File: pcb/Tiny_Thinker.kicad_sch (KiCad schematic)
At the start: 42 parts, among them J2 PERIPHERALS, J3 ADC_TIM, J8 USB_C_Receptacle_USB2.0_16P, SW1 SW_Push, SW2 SW_SPDT, U1 STM32F446RET6, U2 AMS1117-3.3, Y1 16MHz

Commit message: i forgot to save again
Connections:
- net +3.3V: now also J2.10 (Pin_10), J2.18 (Pin_18), J2.38 (Pin_38), J2.9 (Pin_9), J3.37 (Pin_37), J3.40 (Pin_40); no longer J2.13 (Pin_13), J2.14 (Pin_14), J2.25 (Pin_25)
- net CAN1_RX: now also J2.32 (Pin_32); no longer J2.24 (Pin_24)
- net CAN1_TX: now also J2.34 (Pin_34); no longer J2.26 (Pin_26)
- net GND: now also J2.16 (Pin_16), J2.36 (Pin_36), J2.39 (Pin_39), J2.40 (Pin_40), J2.7 (Pin_7), J3.38 (Pin_38), J3.39 (Pin_39); no longer J2.10 (Pin_10), J2.11 (Pin_11), J2.12 (Pin_12), J2.23 (Pin_23), J2.31 (Pin_31), J2.32 (Pin_32)
- net I2C1_SCL: now also J2.23 (Pin_23), J2.24 (Pin_24); no longer J2.15 (Pin_15), J2.16 (Pin_16)
- net I2C1_SDA: now also J2.25 (Pin_25), J2.26 (Pin_26); no longer J2.17 (Pin_17), J2.18 (Pin_18)
- net SPI1_MISO: now also J2.15 (Pin_15); no longer J2.7 (Pin_7)
- net SPI1_MOSI: now also J2.17 (Pin_17); no longer J2.9 (Pin_9)
- net SPI1_NSS: now also J2.11 (Pin_11); no longer J2.3 (Pin_3)
- net SPI1_SCK: now also J2.13 (Pin_13); no longer J2.5 (Pin_5)
- net USB_D+: now also D2.3 (I/O2), J8.A6 (D+), J8.B6 (D+)
- net USB_D-: now also D2.1 (I/O1), J8.A7 (D-), J8.B7 (D-)
- net SPI2_NSS: now reaches U1.33 (PB12)
- net SPI2_NSS: now also J2.37 (Pin_37)
- net SPI2_SCK: now reaches U1.34 (PB13)
- net SPI2_SCK: now also J2.35 (Pin_35)
- net SPI2_MISO: now reaches U1.35 (PB14)
- net SPI2_MISO: now also J2.33 (Pin_33)
- net SPI2_MOSI: now reaches U1.36 (PB15)
- net SPI2_MOSI: now also J2.31 (Pin_31)
- net PA15: now reaches U1.50 (PA15)
- net PA15: now also J2.3 (Pin_3)
- net PC10: now reaches U1.51 (PC10)
- net PC10: now also J2.5 (Pin_5)
- net PC11: now reaches U1.52 (PC11)
- net PC11: now also J2.12 (Pin_12)
- net PC12: now reaches U1.53 (PC12)
- net PC12: now also J2.14 (Pin_14)
- no-connect marks 25 -> 17

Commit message: updated bom / added JLC part #
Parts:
- C16, C17: JLCPCB Part # (none) -> C1623
- D2: JLCPCB Part # (none) -> C7519
- J2, J3: JLCPCB Part # (none) -> C50980
- J8: JLCPCB Part # (none) -> C2765186
- R3: JLCPCB Part # (none) -> C25900
- R4: JLCPCB Part # (none) -> C25531
- R5: JLCPCB Part # (none) -> C17168
- R6, R7: JLCPCB Part # (none) -> C25905
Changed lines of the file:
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@@
 			)
 		)
+		(property "JLCPCB Part #" "C25900"
+			(at 198.12 161.29 0)
+			(effects
+				(font
+					(size 1.27 1.27)
+				)
+				(hide yes)
+			)
+		)
 		(pin "2"
 		)
@@
 			)
 		)
+		(property "JLCPCB Part #" "C2765186"
+			(at 350.52 57.15 0)
+			(effects
+				(font
+					(size 1.27 1.27)
+				)
+				(hide yes)
+			)
+		)
 		(pin "A8"
 		)
@@
 			)
 		)
+		(property "JLCPCB Part #" "C25905"
+			(at 323.85 76.2 0)
+			(effects
+				(font
+					(size 1.27 1.27)
+				)
+				(hide yes)
+			)
+		)
 		(pin "1"
 		)
@@
 			)
 		)
+		(property "JLCPCB Part #" "C25905"
+			(at 332.74 76.2 0)
+			(effects
+				(font
+					(size 1.27 1.27)
+				)
+				(hide yes)
+			)
+		)
 		(pin "1"
 		)
@@
 			)
 		)
+		(property "JLCPCB Part #" "C25531"
+			(at 198.12 171.45 0)
+			(effects
+				(font
+					(size 1.27 1.27)
+				)
+				(hide yes)
+			)
+		)
 		(pin "2"
 		)
@@
 			)
 		)
+		(property "JLCPCB Part #" "C17168"
+			(at 283.21 41.91 90)
+			(effects
+				(font
+					(size 1.27 1.27)
+				)
+				(hide yes)
+			)
+		)
 		(pin "1"
 		)
@@
 			)
 		)
+		(property "JLCPCB Part #" " C7519"
+			(at 320.04 57.15 0)
+			(effects
+				(font
+					(size 1.27 1.27)
+				)
+				(hide yes)
+			)
+		)
 		(pin "3"
 		)
@@
 			)
 		)
+		(property "JLCPCB Part #" " C50980"
+			(at 334.01 181.61 0)
+			(effects
+				(font
+					(size 1.27 1.27)
+				)
+				(hide yes)
+			)
+		)
 		(pin "14"
 		)
@@
 			)
 		)
+		(property "JLCPCB Part #" "C1623"
+			(at 292.1 50.8 0)
+			(effects
+				(font
+					(size 1.27 1.27)
+				)
+				(hide yes)
+			)
+		)
 		(pin "2"
 		)
@@
 			)
 		)
+		(property "JLCPCB Part #" " C50980"
+			(at 265.43 182.88 0)
+			(effects
+				(font
+					(size 1.27 1.27)
+				)
+				(hide yes)
+			)
+		)
 		(pin "14"
 		)
@@
 			(at 274.32 50.8 0)
 			(effects
+				(font
+					(size 1.27 1.27)
+				)
+				(hide yes)
+			)
+		)
+		(property "JLCPCB Part #" "C1623"
+			(at 274.32 50.8 0)
+			(effects

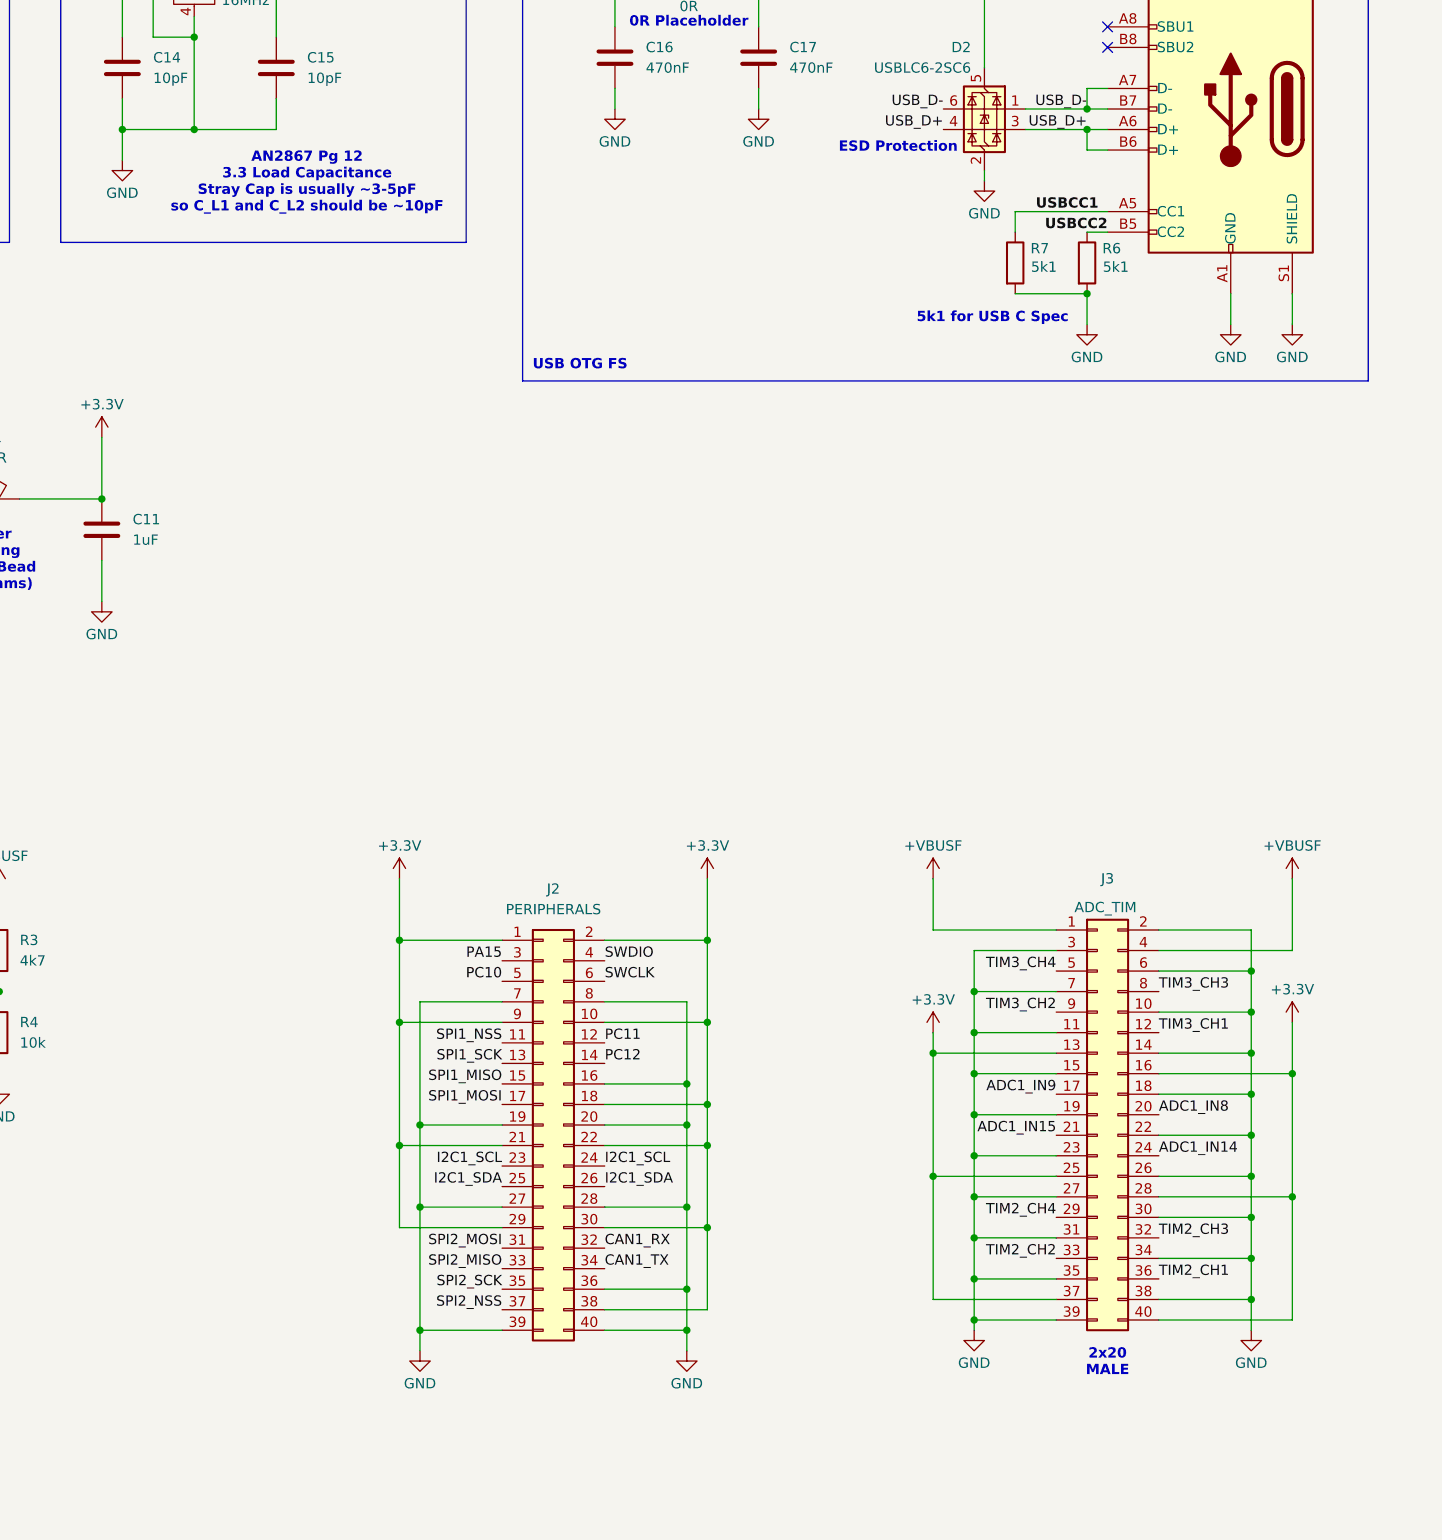
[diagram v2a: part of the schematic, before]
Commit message: Revised JLCPCB capabilities
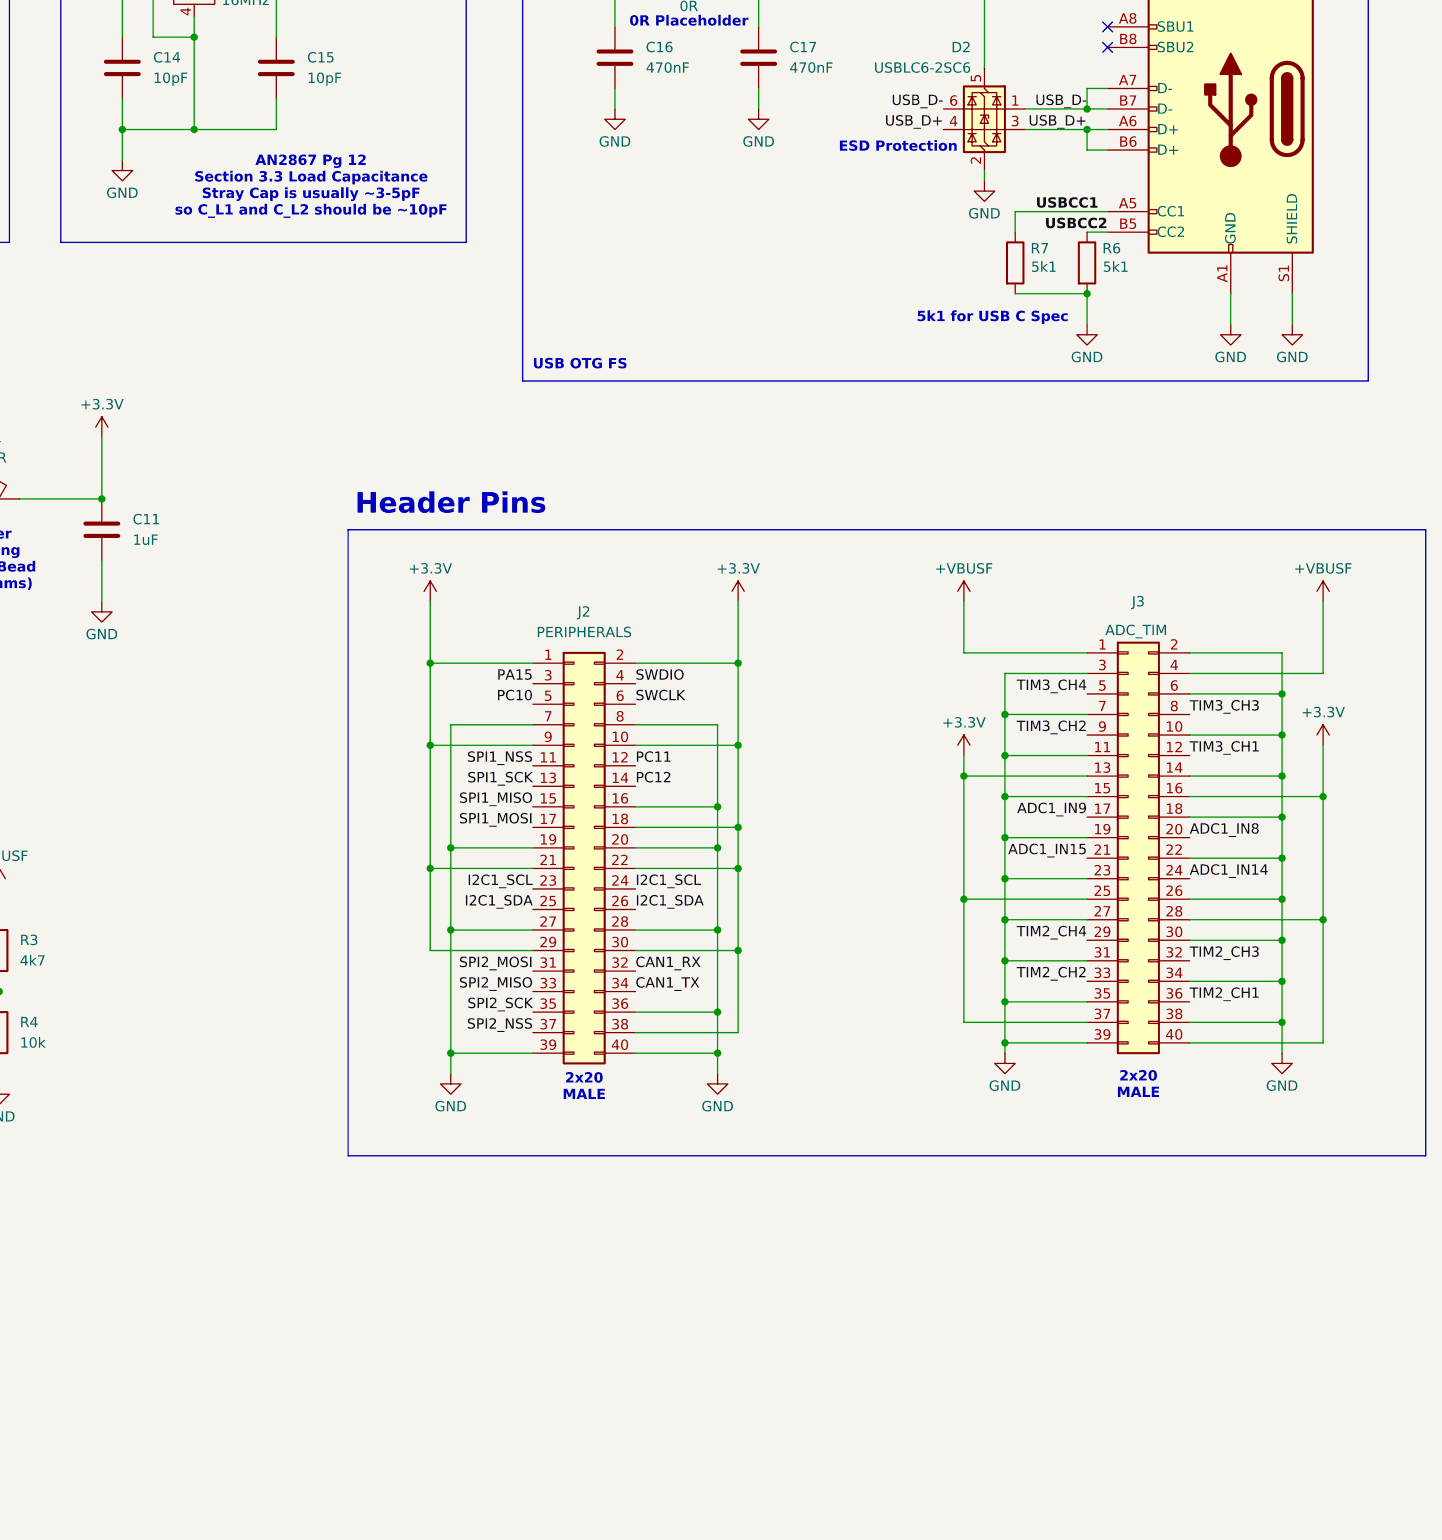
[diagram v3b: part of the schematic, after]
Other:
- note added: "AN2867 Pg 12 Section 3.3 Load Capacitance Stray Cap is usually ~3-5pF so C_L1 and C_L2 should be ~10pF"
- note added: "Header Pins"
- note removed: "AN2867 Pg 12 3.3 Load Capacitance Stray Cap is usually ~3-5pF so C_L1 and C_L2 should be ~10pF"
- moved on the sheet: J2, J3

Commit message: Added more comments
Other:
- note added: "0.6mA using 1.5k Resistor"
- note added: "3.3V - 2.4V = 0.9V 0.9V / 1.5k = 0.6mA"
- note added: "LED Datasheet Forward Voltage ~ 2.4V"
- note added: "try 470 Ohm"
- note removed: "2.2mA using 1.5k Resistor"
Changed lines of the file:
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@@
+		)
+	)
+	(text "try\n470 Ohm"
+		(exclude_from_sim no)
+		(at 191.516 52.578 0)
+		(effects
+			(font
+				(size 1.27 1.27)
+				(thickness 0.254)
+				(bold yes)
+			)
 		)
 	)
@@
 		)
 	)
+	(text "3.3V - 2.4V = 0.9V\n0.9V / 1.5k = 0.6mA"
+		(exclude_from_sim no)
+		(at 188.214 70.866 0)
+		(effects
+			(font
+				(size 1.27 1.27)
+				(thickness 0.254)
+				(bold yes)
+			)
+		)
+	)
 	(text "M2"
 		(exclude_from_sim no)
@@
 		)
 	)
-	(text "2.2mA using\n1.5k Resistor"
+	(text "LED Datasheet\nForward Voltage\n~ 2.4V"
+		(exclude_from_sim no)
+		(at 179.324 29.21 0)
+		(effects
+			(font
+				(size 1.27 1.27)
+				(thickness 0.254)
+				(bold yes)
+			)
+		)
+	)
+	(text "0.6mA using\n1.5k Resistor"
 		(exclude_from_sim no)
 		(at 177.546 45.72 0)

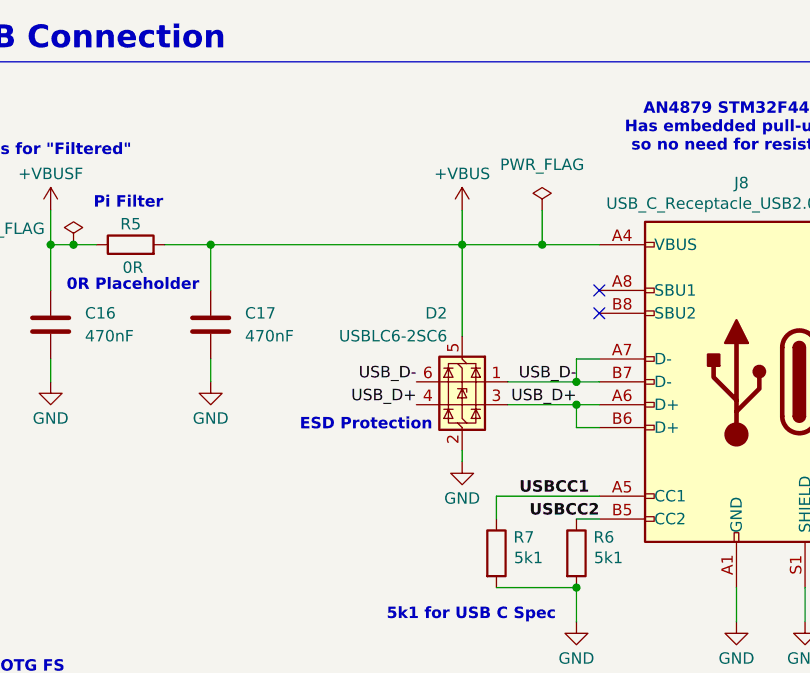
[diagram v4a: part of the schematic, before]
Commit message: renamed USB C net labels
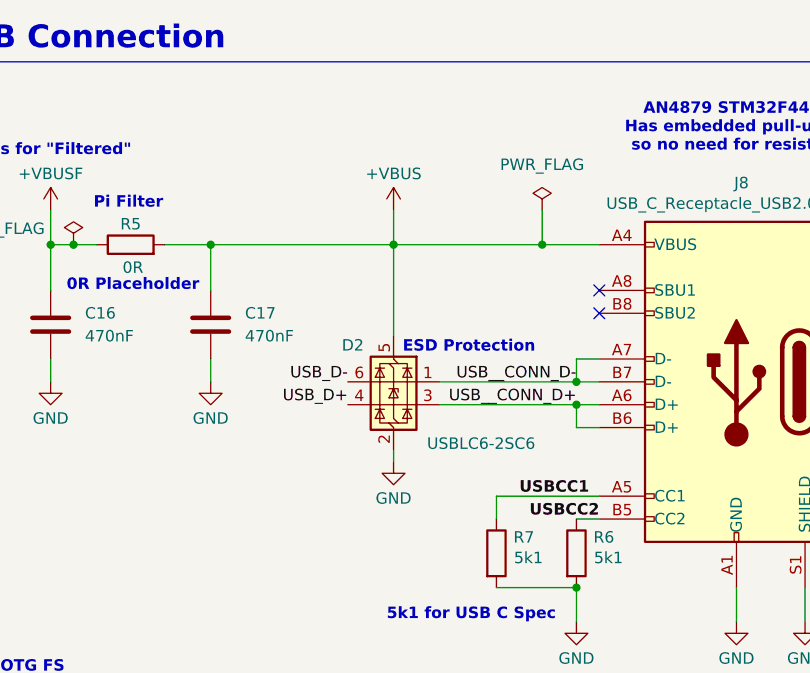
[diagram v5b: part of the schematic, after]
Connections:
- net USB_D+: no longer D2.3 (I/O2), J8.A6 (D+), J8.B6 (D+)
- net USB_D-: no longer D2.1 (I/O1), J8.A7 (D-), J8.B7 (D-)
- new net USB__CONN_D+: D2.3 (I/O2), J8.A6 (D+), J8.B6 (D+)
- new net USB__CONN_D-: D2.1 (I/O1), J8.A7 (D-), J8.B7 (D-)
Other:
- moved on the sheet: D2

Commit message: Added user led
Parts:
- added D3: BLUE, LED_SMD:LED_0603_1608Metric, symbol Device:LED
- added R8: 1k5, Resistor_SMD:R_0402_1005Metric, symbol Device:R
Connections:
- net GND: now also R8.2
- net TIM2_CH1: now also J3.32 (Pin_32); no longer J3.36 (Pin_36)
- net TIM2_CH3: now also J3.36 (Pin_36); no longer J3.32 (Pin_32)
- net GPIO_USER_LED: now reaches U1.9 (PC1)
- net GPIO_USER_LED: now also D3.2 (A)
- new net USER_LED_K: D3.1 (K), R8.1
- no-connect marks 17 -> 16
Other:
- note added: "USER LED"
- moved on the sheet: R1, SW2

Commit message: cleaned up routing
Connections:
- net GPIO_USER_LED renamed GPIO_USER_LED_B
- net USER_LED_K renamed USER_LED_B_K
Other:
- note added: "USER LEDS"
- note removed: "USER LED"
- moved on the sheet: D3, R8
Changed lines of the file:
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@@
 		)
 	)
-	(text "USER LED"
+	(text "USER LEDS\n"
 		(exclude_from_sim no)
-		(at 104.14 188.214 0)
+		(at 105.664 188.976 0)
 		(effects
 			(font
@@
 	)
 	(no_connect
-		(at 128.27 171.45)
-	)
-	(no_connect
 		(at 128.27 204.47)
 	)
@@
 		(at 128.27 201.93)
 	)
+	(no_connect
+		(at 128.27 171.45)
+	)
 	(wire
 		(pts
@@
 	(wire
 		(pts
-			(xy 96.52 195.58) (xy 96.52 199.39)
+			(xy 92.71 195.58) (xy 92.71 199.39)
 		)
 		(stroke
@@
 	(wire
 		(pts
+			(xy 104.14 182.88) (xy 110.49 182.88)
+		)
+		(stroke
+			(width 0)
+			(type default)
+		)
+	)
+	(wire
+		(pts
 			(xy 213.36 31.75) (xy 240.03 31.75)
 		)
@@
 	(wire
 		(pts
-			(xy 96.52 182.88) (xy 96.52 187.96)
+			(xy 92.71 182.88) (xy 92.71 187.96)
 		)
 		(stroke
@@
 	(wire
 		(pts
-			(xy 110.49 182.88) (xy 107.95 182.88)
-		)
-		(stroke
-			(width 0)
-			(type default)
-		)
-	)
-	(wire
-		(pts
 			(xy 322.58 152.4) (xy 332.74 152.4)
 		)
@@
 	(wire
 		(pts
-			(xy 100.33 182.88) (xy 96.52 182.88)
+			(xy 96.52 182.88) (xy 92.71 182.88)
 		)
 		(stroke
@@
 		)
 	)
-	(label "GPIO_USER_LED"
+	(label "GPIO_USER_LED_B"
 		(at 128.27 168.91 180)
 		(effects
@@
 		)
 	)
-	(label "USER_LED_K"
-		(at 100.33 182.88 180)
+	(label "USER_LED_B_K"
+		(at 96.52 182.88 180)
 		(effects
 			(font
@@
 	(symbol
 		(lib_id "Device:LED")
-		(at 104.14 182.88 0)
+		(at 100.33 182.88 0)
 		(mirror x)
 		(unit 1)
@@
 		(dnp no)
 		(property "Reference" "D3"
-			(at 104.14 185.928 0)
+			(at 100.33 185.928 0)
 			(effects
 				(font
@@
 		)
 		(property "Value" "BLUE"
-			(at 104.394 179.832 0)
+			(at 100.584 179.832 0)
 			(effects
 				(font
@@
 		)
 		(property "Footprint" "LED_SMD:LED_0603_1608Metric"
-			(at 104.14 182.88 0)
+			(at 100.33 182.88 0)
 			(effects
 				(font
@@
 		)
 		(property "Datasheet" "~"
-			(at 104.14 182.88 0)
+			(at 100.33 182.88 0)
 			(effects
 				(font
@@
 		)
 		(property "Description" "Light emitting diode"
-			(at 104.14 182.88 0)
+			(at 100.33 182.88 0)
 			(effects
 				(font
@@
 		)
 		(property "Sim.Pins" "1=K 2=A"
-			(at 104.14 182.88 0)
+			(at 100.33 182.88 0)
 			(effects
 				(font
@@
 		)
 		(property "JLCPCB Part #" "C2288"
-			(at 104.14 182.88 0)
+			(at 100.33 182.88 0)
 			(effects
 				(font
@@
 	(symbol
 		(lib_id "Device:R")
-		(at 96.52 191.77 0)
+		(at 92.71 191.77 0)
 		(unit 1)
 		(exclude_from_sim no)
@@
 		(fields_autoplaced yes)
 		(property "Reference" "R8"
-			(at 99.06 190.4999 0)
+			(at 95.25 190.4999 0)
 			(effects
 				(font
@@
 		)
 		(property "Value" "1k5"
-			(at 99.06 193.0399 0)
+			(at 95.25 193.0399 0)
 			(effects
 				(font
@@
 		)
 		(property "Footprint" "Resistor_SMD:R_0402_1005Metric"
-			(at 94.742 191.77 90)
+			(at 90.932 191.77 90)
 			(effects
 				(font
@@
 		)
 		(property "Datasheet" "~"
-			(at 96.52 191.77 0)
+			(at 92.71 191.77 0)
 			(effects
 				(font
@@
 		)
 		(property "Description" "Resistor"
-			(at 96.52 191.77 0)
+			(at 92.71 191.77 0)
 			(effects
 				(font
@@
 		)
 		(property "JLCPCB Part #" "C25867"
-			(at 96.52 191.77 0)
+			(at 92.71 191.77 0)
 			(effects
 				(font
@@
 	(symbol
 		(lib_id "power:GND")
-		(at 96.52 199.39 0)
+		(at 92.71 199.39 0)
 		(unit 1)
 		(exclude_from_sim no)
@@
 		(dnp no)
 		(property "Reference" "#PWR027"
-			(at 96.52 205.74 0)
+			(at 92.71 205.74 0)
 			(effects
 				(font
@@
 		)
 		(property "Value" "GND"
-			(at 96.52 203.454 0)
+			(at 92.71 203.454 0)
 			(effects
 				(font
@@
 		)
 		(property "Footprint" ""
-			(at 96.52 199.39 0)
+			(at 92.71 199.39 0)
 			(effects
 				(font
@@
 		)
 		(property "Datasheet" ""
-			(at 96.52 199.39 0)
+			(at 92.71 199.39 0)
 			(effects
 				(font
@@
 		)
 		(property "Description" "Power symbol creates a global label with name \"GND\" , ground"
-			(at 96.52 199.39 0)
+			(at 92.71 199.39 0)
 			(effects
 				(font

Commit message: added and routed TPS2116 Power OR-ing IC
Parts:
- added C18, C19, C20: 10uF, Capacitor_SMD:C_0603_1608Metric, symbol Device:C
- added R10, R9: 100k, Resistor_SMD:R_0603_1608Metric, symbol Device:R
- added U3: TPS2116DRL, Package_TO_SOT_SMD:SOT-583-8, symbol Power_Management:TPS2116DRL
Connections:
- net +VBUSF: now also C18.1, R9.1, U3.3 (VIN1), U3.5 (MODE); no longer C12.1, U2.3 (VI)
- net GND: now also C18.2, C19.2, C20.2, R10.2, U3.1 (GND)
- net USB__CONN_D+ renamed USB_CONN_D+
- net USB__CONN_D- renamed USB_CONN_D-
- new net +5V_EXT: C19.1, U3.6 (VIN2)
- new net +5V_SYS: C12.1, C20.1, U2.3 (VI), U3.2 (VOUT), U3.7 (VOUT)
- new net PR1: R10.1, R9.2, U3.4 (PR1)
- no-connect marks 16 -> 17
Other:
- note added: "MODE tied to VIN1 -> Priority Mode PR1 High -> VOUT = VIN1 PR1 Low -> VOUT = VIN2"
- note added: "Power OR-ing"
